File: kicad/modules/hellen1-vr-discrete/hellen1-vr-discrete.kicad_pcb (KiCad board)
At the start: 2 copper layers, 18.2 x 17 mm, 45 parts, among them M1 Module-vr-discrete-0.1, U1 74AHC1G02, U2 74AHC1G02, U751 SRV05-4, U753 MCP6004, U754 MAX9142, U755 NC7SB3157P6X, U756 NC7SB3157P6X

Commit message: vr-discrete: rename SRV05-4-P-T7 in kicad
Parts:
- U751: value SRV05-4 -> SRV05-4-P-T7
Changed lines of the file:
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@@
       (effects (font (size 1 1) (thickness 0.15)))
     )
-    (fp_text value "SRV05-4" (at 0 2.4) (layer "F.Fab")
+    (fp_text value "SRV05-4-P-T7" (at 0 2.4) (layer "F.Fab")
       (effects (font (size 1 1) (thickness 0.15)))
     )

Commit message: fix BOM/LED-GREEN-0603 for vr-discrete
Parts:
- D751: value LED -> LED-GREEN-0603
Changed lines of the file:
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@@
       (effects (font (size 1 1) (thickness 0.15)))
     )
-    (fp_text value "LED" (at 0 1.43) (layer "F.Fab")
+    (fp_text value "LED-GREEN-0603" (at 0 1.43) (layer "F.Fab")
       (effects (font (size 1 1) (thickness 0.15)))
     )

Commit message: vr-discrete: fix designator numbering
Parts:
- removed C1: 1u, Capacitor_SMD:C_0402_1005Metric
- removed M1: Module-vr-discrete-0.1, hellen-one-vr-discrete-0.1:vr-discrete
- removed U1, U2: 74AHC1G02, Package_TO_SOT_SMD:SOT-23-5
- added C761: 1u, Capacitor_SMD:C_0402_1005Metric, F.Cu at (86.6, 82.7)
- added M750: Module-vr-discrete-0.1, hellen-one-vr-discrete-0.1:vr-discrete, F.Cu at (77.7, 95.0)
- added U752: 74AHC1G02, Package_TO_SOT_SMD:SOT-23-5, F.Cu at (82.8, 80.4)
- added U757: 74AHC1G02, Package_TO_SOT_SMD:SOT-23-5, F.Cu at (87.0, 80.4)
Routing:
- net Net-(U1-Pad2): track 4.97 -> 0.00 mm
- net (no net): track 0.00 -> 4.97 mm

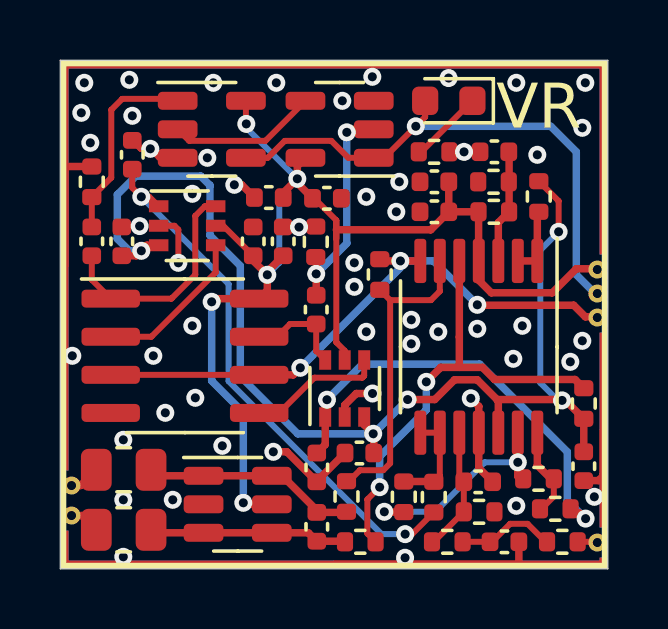
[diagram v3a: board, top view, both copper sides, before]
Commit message: Перепланировка на двусторонний монтаж
4 layers

Update hellen1-vr-discrete.kicad_pcb

Обновила контур, доработка внутри

класс цепей

сквозные пады GND
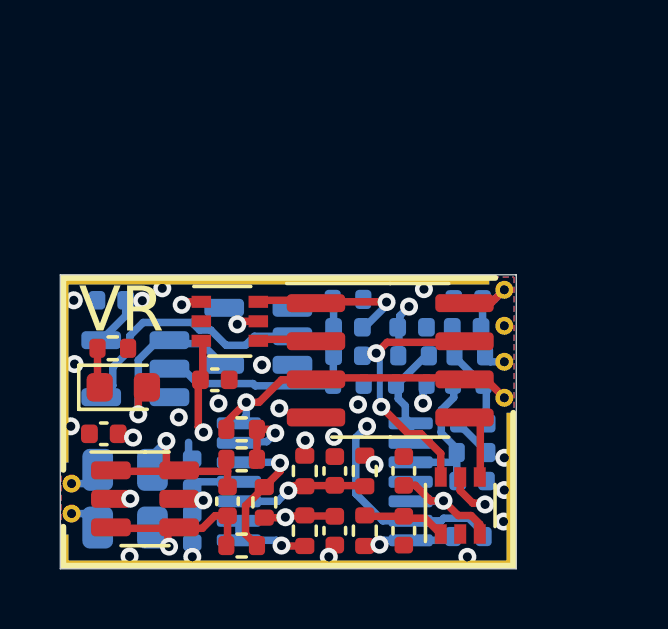
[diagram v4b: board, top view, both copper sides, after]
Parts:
- C752, C753, C755, C756, C757, C760, C761, C762, C764, C766, R752, R753, R754, R757, R760, R761, R762, R763, R765, R766, U752, U753, U757: moved to B.Cu
- moved D751 14.5 mm to (79.8, 89.0), turned to 0 degrees
- moved R769 13.6 mm to (85.8, 93.8)
- moved C760 13.3 mm to (82.1, 93.7), turned to -90 degrees
- moved C762 12.6 mm to (82.1, 91.9), turned to 90 degrees
- moved R751 12.6 mm to (79.5, 87.7)
- moved C759 11.9 mm to (86.8, 91.8), turned to 90 degrees
- moved R758 11.1 mm to (84.5, 92.8)
- moved C755 11.0 mm to (89.4, 87.0), turned to 0 degrees
- moved R767 10.7 mm to (85.8, 91.8), turned to -90 degrees
- moved R768 10.6 mm to (87.8, 91.8), turned to 90 degrees
- moved U757 10.5 mm to (80.2, 88.4)
- moved C763 9.61 mm to (79.2, 90.5)
- moved R765 9.40 mm to (87.3, 86.1), turned to 180 degrees
- moved C756 9.01 mm to (87.3, 87.0), turned to 0 degrees
- moved C754 8.57 mm to (86.8, 93.8)
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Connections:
- U752 pad 2: (no net) -> Net-(U752-Pad2)
- U757 pad 4: (no net) -> Net-(U752-Pad2)
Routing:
- net GND: track 25.5 -> 1.98 mm, vias 52 -> 20
- net Vref: track 39.4 -> 19.4 mm, vias 5 -> 3
- net thresh_high: track 14.8 -> 2.70 mm, vias 2 -> 0
- net Net-(R756-Pad2): track 15.5 -> 4.77 mm, vias 2 -> 1
- net +5V: track 42.6 -> 52.5 mm, vias 5 -> 6
- net analog_out: track 20.1 -> 11.1 mm, vias 3 -> 1
- net Net-(U752-Pad2): track 0.00 -> 8.69 mm
- net thresh_low: track 18.4 -> 10.4 mm
- net Net-(R755-Pad1): track 10.4 -> 2.96 mm, vias 0 -> 1
- net Net-(C757-Pad2): track 3.40 -> 8.67 mm, vias 0 -> 2
- net (no net): track 4.97 -> 0.00 mm
- net Net-(C756-Pad1): track 6.56 -> 2.14 mm
- net Net-(U754-Pad2): track 5.29 -> 1.86 mm
- net Net-(C756-Pad2): track 8.44 -> 5.03 mm, vias 0 -> 1
- net output: track 18.4 -> 21.3 mm
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- added copper zone on In1.Cu, net GND
- added copper zone on In2.Cu, net GND
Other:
- board size 18.2 x 17 mm -> 15.2 x 9.8 mm
- copper layers 2 -> 4

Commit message: add VR 0.2
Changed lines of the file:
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@@
   (gr_rect (start 77.7 95.05) (end 92.9 85.25) (layer "Edge.Cuts") (width 0.02) (fill none))
   (gr_rect (start 77.7 95.05) (end 92.9 85.25) (layer "User.1") (width 0.02) (fill none))
-  (gr_text "VR" (at 79.735274 86.410274) (layer "F.SilkS")
+  (gr_text "VR" (at 79.724999 86.475135) (layer "F.SilkS")
     (effects (font (size 1.5 1.5) (thickness 0.2)))
   )
@@
   (segment (start 82.342385 87.092385) (end 82.089116 86.839116) (width 0.25) (layer "B.Cu") (net 29))
   (segment (start 85.6375 87.3) (end 84.169298 87.3) (width 0.25) (layer "B.Cu") (net 29))
+  (zone (net 0) (net_name "") (layers "F.Cu" "In1.Cu" "In2.Cu" "B.Cu") (hatch edge 0.508)
+    (connect_pads (clearance 0))
+    (min_thickness 0.254)
+    (keepout (tracks allowed) (vias allowed) (pads allowed) (copperpour not_allowed) (footprints allowed))
+    (fill (thermal_gap 0.508) (thermal_bridge_width 0.508))
+    (polygon
+      (pts
+        (xy 92.85 89.35)
+        (xy 92.2 89.35)
+        (xy 92.2 85.325)
+        (xy 92.825 85.325)
+      )
+    )
+  )
   (zone (net 1) (net_name "GND") (layers "F.Cu" "In1.Cu" "In2.Cu" "B.Cu") (hatch edge 0.508)
     (connect_pads (clearance 0))

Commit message: VR 0.2 progress
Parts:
- M750: value Module-vr-discrete-0.1 -> Module-vr-discrete-0.2; footprint hellen-one-vr-discrete-0.1:vr-discrete -> hellen-one-vr-discrete-0.2:vr-discrete
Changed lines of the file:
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@@
     )
   )
-  (footprint "hellen-one-vr-discrete-0.1:vr-discrete" locked (layer "F.Cu")
+  (footprint "hellen-one-vr-discrete-0.2:vr-discrete" (layer "F.Cu")
     (at 77.7 95.05)
     (property "Sheetfile" "Файл: hellen1-vr-discrete.kicad_sch")
@@
       (effects (font (size 1 1) (thickness 0.15)))
     )
-    (fp_text value "Module-vr-discrete-0.1" (at 9.02 -16 unlocked) (layer "F.Fab") hide
+    (fp_text value "Module-vr-discrete-0.2" (at 9.02 -16 unlocked) (layer "F.Fab") hide
       (effects (font (size 1 1) (thickness 0.15)))
     )
     (fp_line (start 0.1 -9.7) (end 0.1 -3.3) (layer "B.SilkS") (width 0.2))
+    (fp_line (start 14.5 -9.7) (end 0.1 -9.7) (layer "B.SilkS") (width 0.2))
+    (fp_line (start 15.1 -0.1) (end 15.1 -5.2) (layer "B.SilkS") (width 0.2))
     (fp_line (start 0.1 -0.1) (end 15.1 -0.1) (layer "B.SilkS") (width 0.2))
-    (fp_line (start 15.1 -0.1) (end 15.1 -5.2) (layer "B.SilkS") (width 0.2))
     (fp_line (start 0.1 -0.1) (end 0.1 -1.4) (layer "B.SilkS") (width 0.2))
-    (fp_line (start 14.5 -9.7) (end 0.1 -9.7) (layer "B.SilkS") (width 0.2))
-    (fp_line (start 15.1 -0.1) (end 15.1 -5.2) (layer "F.SilkS") (width 0.2))
+    (fp_line (start 0.1 -0.1) (end 0.1 -1.4) (layer "F.SilkS") (width 0.2))
     (fp_line (start 14.5 -9.7) (end 0.1 -9.7) (layer "F.SilkS") (width 0.2))
     (fp_line (start 0.1 -0.1) (end 15.1 -0.1) (layer "F.SilkS") (width 0.2))
     (fp_line (start 0.1 -9.7) (end 0.1 -3.3) (layer "F.SilkS") (width 0.2))
-    (fp_line (start 0.1 -0.1) (end 0.1 -1.4) (layer "F.SilkS") (width 0.2))
-    (pad "E1" thru_hole circle locked (at 14.8 -6.9 180) (size 0.6 0.6) (drill 0.3) (layers *.Cu *.Mask)
+    (fp_line (start 15.1 -0.1) (end 15.1 -5.2) (layer "F.SilkS") (width 0.2))
+    (pad "E1" thru_hole circle (at 14.8 -6.9 180) (size 0.6 0.6) (drill 0.3) (layers *.Cu *.Mask)
       (net 18 "thresh_input") (pinfunction "Thresh_IN") (pintype "passive") (solder_paste_margin -49.999999) (zone_connect 2))
-    (pad "E2" thru_hole circle locked (at 14.8 -5.7 180) (size 0.6 0.6) (drill 0.3) (layers *.Cu *.Mask)
+    (pad "E2" thru_hole circle (at 14.8 -5.7 180) (size 0.6 0.6) (drill 0.3) (layers *.Cu *.Mask)
       (net 17 "analog_out") (pinfunction "OUT_A") (pintype "passive") (solder_paste_margin -49.999999) (zone_connect 2))
-    (pad "E3" thru_hole circle locked (at 14.8 -8.1 180) (size 0.6 0.6) (drill 0.3) (layers *.Cu *.Mask)
+    (pad "E3" thru_hole circle (at 14.8 -8.1 180) (size 0.6 0.6) (drill 0.3) (layers *.Cu *.Mask)
       (net 16 "output") (pinfunction "OUT") (pintype "passive") (solder_paste_margin -49.999999) (zone_connect 2))
-    (pad "E4" thru_hole circle locked (at 14.8 -9.3 180) (size 0.6 0.6) (drill 0.3) (layers *.Cu *.Mask)
+    (pad "E4" thru_hole circle (at 14.8 -9.3 180) (size 0.6 0.6) (drill 0.3) (layers *.Cu *.Mask)
       (net 6 "+5V") (pinfunction "V5_IN") (pintype "passive") (solder_paste_margin -49.999999) (zone_connect 2))
-    (pad "G" thru_hole rect locked (at 0.15 -0.5825) (size 0.25 1.115) (layers *.Cu *.Mask)
-      (net 1 "GND") (pinfunction "GND") (pintype "passive") (solder_mask_margin -1) (zone_connect 2))
-    (pad "G" thru_hole rect locked (at 0.15 -6.6325) (size 0.25 6.185) (layers *.Cu *.Mask)
-      (net 1 "GND") (pinfunction "GND") (pintype "passive") (solder_mask_margin -1) (zone_connect 2))
-    (pad "G" thru_hole rect locked (at 7.1625 -9.6 90) (size 0.25 14.275) (layers *.Cu *.Mask)
-      (net 1 "GND") (pinfunction "GND") (pintype "passive") (solder_mask_margin -1) (zone_connect 2))
-    (pad "G" smd rect locked (at 15 -2.6125) (size 0.25 5.175) (layers "B.Cu")
-      (net 1 "GND") (pinfunction "GND") (pintype "passive") (solder_mask_margin -1) (zone_connect 2))
-    (pad "G" smd rect locked (at 7.1625 -9.6 90) (size 0.25 14.275) (layers "B.Cu")
-      (net 1 "GND") (pinfunction "GND") (pintype "passive") (solder_mask_margin -1) (zone_connect 2))
-    (pad "G" smd rect locked (at 0.15 -6.6325) (size 0.25 6.185) (layers "B.Cu")
-      (net 1 "GND") (pinfunction "GND") (pintype "passive") (solder_mask_margin -1) (zone_connect 2))
-    (pad "G" smd rect locked (at 0.15 -0.5825) (size 0.25 1.115) (layers "B.Cu")
-      (net 1 "GND") (pinfunction "GND") (pintype "passive") (solder_mask_margin -1) (zone_connect 2))
-    (pad "G" thru_hole rect locked (at 7.575 -0.15 90) (size 0.25 15.1) (layers *.Cu *.Mask)
-      (net 1 "GND") (pinfunction "GND") (pintype "passive") (solder_mask_margin -1) (zone_connect 2))
-    (pad "G" smd rect locked (at 7.575 -0.15 90) (size 0.25 15.1) (layers "B.Cu")
-      (net 1 "GND") (pinfunction "GND") (pintype "passive") (solder_mask_margin -1) (zone_connect 2))
-    (pad "G" thru_hole rect locked (at 15 -2.6125) (size 0.25 5.175) (layers *.Cu *.Mask)
-      (net 1 "GND") (pinfunction "GND") (pintype "passive") (solder_mask_margin -1) (zone_connect 2))
-    (pad "W1" thru_hole circle locked (at 0.375 -2.84 180) (size 0.6 0.6) (drill 0.3) (layers *.Cu *.Mask)
+    (pad "G" smd rect (at 15 -2.6125) (size 0.25 5.175) (layers "B.Cu")
+      (net 1 "GND") (pinfunction "GND") (pintype "passive") (zone_connect 2))
+    (pad "G" smd rect (at 0.15 -0.5825) (size 0.25 1.115) (layers "In1.Cu")
+      (net 1 "GND") (pinfunction "GND") (pintype "passive") (zone_connect 2))
+    (pad "G" smd rect (at 7.1625 -9.6 90) (size 0.25 14.275) (layers "In2.Cu")
+      (net 1 "GND") (pinfunction "GND") (pintype "passive") (zone_connect 2))
+    (pad "G" smd rect (at 0.15 -0.5825) (size 0.25 1.115) (layers "F.Cu")
+      (net 1 "GND") (pinfunction "GND") (pintype "passive") (zone_connect 2))
+    (pad "G" smd rect (at 15 -2.6125) (size 0.25 5.175) (layers "In2.Cu")
+      (net 1 "GND") (pinfunction "GND") (pintype "passive") (zone_connect 2))
+    (pad "G" smd rect (at 0.15 -6.6325) (size 0.25 6.185) (layers "F.Cu")
+      (net 1 "GND") (pinfunction "GND") (pintype "passive") (zone_connect 2))
+    (pad "G" smd rect (at 7.1625 -9.6 90) (size 0.25 14.275) (layers "In1.Cu")
+      (net 1 "GND") (pinfunction "GND") (pintype "passive") (zone_connect 2))
+    (pad "G" smd rect (at 0.15 -0.5825) (size 0.25 1.115) (layers "B.Cu")
+      (net 1 "GND") (pinfunction "GND") (pintype "passive") (zone_connect 2))
+    (pad "G" smd rect (at 0.15 -6.6325) (size 0.25 6.185) (layers "In1.Cu")
+      (net 1 "GND") (pinfunction "GND") (pintype "passive") (zone_connect 2))
+    (pad "G" smd rect (at 7.575 -0.15 90) (size 0.25 15.1) (layers "In2.Cu")
+      (net 1 "GND") (pinfunction "GND") (pintype "passive") (zone_connect 2))
+    (pad "G" smd rect (at 15 -2.6125) (size 0.25 5.175) (layers "In1.Cu")
+      (net 1 "GND") (pinfunction "GND") (pintype "passive") (zone_connect 2))
+    (pad "G" smd rect (at 7.1625 -9.6 90) (size 0.25 14.275) (layers "B.Cu")
+      (net 1 "GND") (pinfunction "GND") (pintype "passive") (zone_connect 2))
+    (pad "G" smd rect (at 0.15 -0.5825) (size 0.25 1.115) (layers "In2.Cu")
+      (net 1 "GND") (pinfunction "GND") (pintype "passive") (zone_connect 2))
+    (pad "G" smd rect (at 7.575 -0.15 90) (size 0.25 15.1) (layers "F.Cu")
+      (net 1 "GND") (pinfunction "GND") (pintype "passive") (zone_connect 2))
+    (pad "G" smd rect (at 0.15 -6.6325) (size 0.25 6.185) (layers "In2.Cu")
+      (net 1 "GND") (pinfunction "GND") (pintype "passive") (zone_connect 2))
+    (pad "G" smd rect (at 15 -2.6125) (size 0.25 5.175) (layers "F.Cu")
+      (net 1 "GND") (pinfunction "GND") (pintype "passive") (zone_connect 2))
+    (pad "G" smd rect (at 7.575 -0.15 90) (size 0.25 15.1) (layers "In1.Cu")
+      (net 1 "GND") (pinfunction "GND") (pintype "passive") (zone_connect 2))
+    (pad "G" smd rect (at 0.15 -6.6325) (size 0.25 6.185) (layers "B.Cu")
+      (net 1 "GND") (pinfunction "GND") (pintype "passive") (zone_connect 2))
+    (pad "G" smd rect (at 7.1625 -9.6 90) (size 0.25 14.275) (layers "F.Cu")
+      (net 1 "GND") (pinfunction "GND") (pintype "passive") (zone_connect 2))
+    (pad "G" smd rect (at 7.575 -0.15 90) (size 0.25 15.1) (layers "B.Cu")
+      (net 1 "GND") (pinfunction "GND") (pintype "passive") (zone_connect 2))
+    (pad "W1" thru_hole circle (at 0.375 -2.84 180) (size 0.6 0.6) (drill 0.3) (layers *.Cu *.Mask)
       (net 19 "VR-") (pinfunction "VR-") (pintype "passive") (solder_paste_margin -49.999999) (zone_connect 2))
-    (pad "W2" thru_hole circle locked (at 0.375 -1.84 180) (size 0.6 0.6) (drill 0.3) (layers *.Cu *.Mask)
+    (pad "W2" thru_hole circle (at 0.375 -1.84 180) (size 0.6 0.6) (drill 0.3) (layers *.Cu *.Mask)
       (net 20 "VR+") (pinfunction "VR+") (pintype "passive") (solder_paste_margin -49.999999) (zone_connect 2))
   )
